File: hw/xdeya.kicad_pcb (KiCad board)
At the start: 2 copper layers, 86.2 x 48.5 mm, 75 parts, among them J2 display, J3 antenna, J4 USB_B_Micro, J5 battery, J6 A, J7 K, Q1 ML5203, Q2 ML5203, Q3 S8050, Q4 S8050, SW3 btn-up, SW4 btn-sel, SW5 btn-down, U1 ESP32-WROOM-32, U2 MCP73831, U3 MIC5219-3.3, U4 BMP280, U5 PCF8563T, U6 NEO-M8N, U7 CP2102, U8 LSM303DLH, U9 XC6206P182MR, Y1 32768

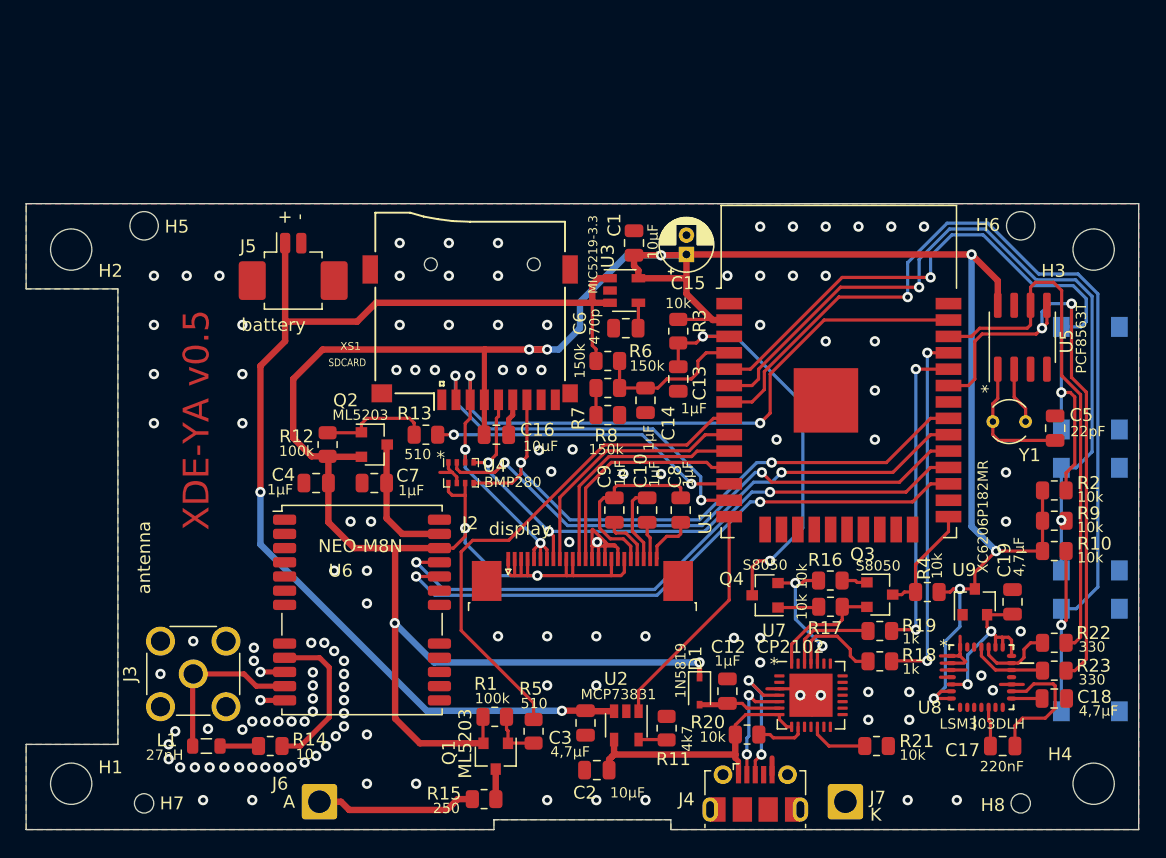
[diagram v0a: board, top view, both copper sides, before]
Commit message: hw - обновление kikad до v7
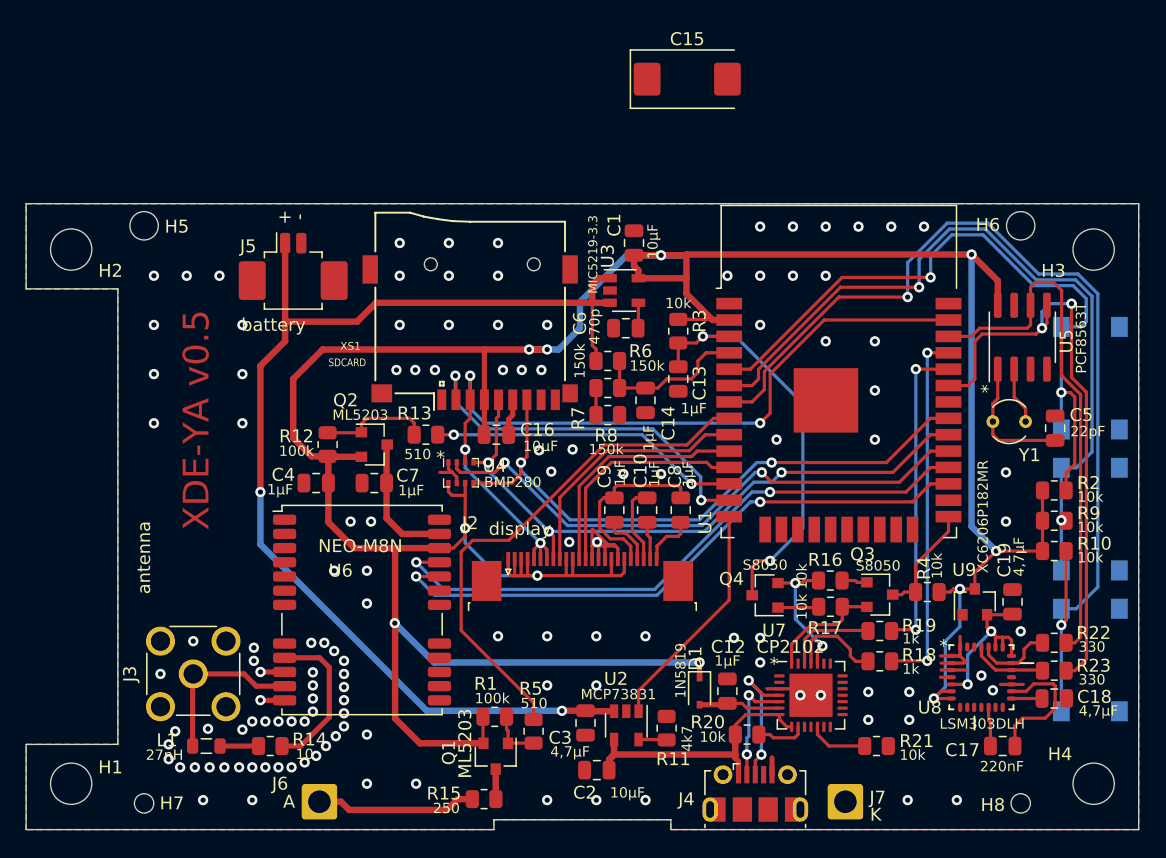
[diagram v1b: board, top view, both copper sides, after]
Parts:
- C15: value CP -> 330uf; footprint Capacitor_THT:CP_Radial_D4.0mm_P1.50mm -> Capacitor_Tantalum_SMD:CP_EIA-7343-20_Kemet-V
- moved C15 13.6 mm to (101.0, 27.9), turned to 0 degrees
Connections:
- C1 pad 1: +3V3 -> +3.3V
- C13 pad 1: /s-en -> +3.3V
- C15 pad 1: +3V3 -> +3.3V
- C16 pad 1: +3V3 -> +3.3V
- C4 pad 1: +3V3 -> +3.3V
- D1 pad 1: +3V3 -> +3.3V
- J2 pad 1: +3V3 -> +3.3V
- J2 pad 10: +3V3 -> +3.3V
- J2 pad 11: +3V3 -> +3.3V
- J2 pad 17: +3V3 -> +3.3V
- J2 pad 19: +3V3 -> +3.3V
- J2 pad 2: +3V3 -> +3.3V
- J2 pad 3: +3V3 -> +3.3V
- J2 pad 4: +3V3 -> +3.3V
- J4 pad 4: Net-(J4-Pad4) -> unconnected-(J4-ID-Pad4)
- Q1 pad 2: +3V3 -> +3.3V
- Q2 pad 2: +3V3 -> +3.3V
- Q4 pad 2: Net-(Q4-Pad2) -> Net-(Q4-E)
- Q4 pad 3: /s-en -> +3.3V
- R1 pad 1: +3V3 -> +3.3V
- R10 pad 1: +3V3 -> +3.3V
- R12 pad 1: +3V3 -> +3.3V
- R16 pad 2: Net-(Q4-Pad2) -> Net-(Q4-E)
- R18 pad 1: Net-(R18-Pad1) -> Net-(U7-~{RTS})
- R19 pad 1: Net-(R19-Pad1) -> Net-(U7-~{CTS})
- R2 pad 1: +3V3 -> +3.3V
- R20 pad 2: Net-(R20-Pad2) -> unconnected-(R20-Pad2)
- R21 pad 1: Net-(R21-Pad1) -> Net-(U7-~{SUSPEND})
- R3 pad 1: +3V3 -> +3.3V
- R3 pad 2: /s-en -> +3.3V
- R4 pad 1: +3V3 -> +3.3V
- R9 pad 1: +3V3 -> +3.3V
- U1 pad 16: Net-(U1-Pad16) -> unconnected-(U1-IO13-Pad16)
- U1 pad 17: Net-(U1-Pad17) -> unconnected-(U1-SHD/SD2-Pad17)
- U1 pad 18: Net-(U1-Pad18) -> unconnected-(U1-SWP/SD3-Pad18)
- U1 pad 19: Net-(U1-Pad19) -> unconnected-(U1-SCS/CMD-Pad19)
- U1 pad 2: +3V3 -> +3.3V
- U1 pad 20: Net-(U1-Pad20) -> unconnected-(U1-SCK/CLK-Pad20)
- U1 pad 21: Net-(U1-Pad21) -> unconnected-(U1-SDO/SD0-Pad21)
- U1 pad 22: Net-(U1-Pad22) -> unconnected-(U1-SDI/SD1-Pad22)
- U1 pad 23: Net-(U1-Pad23) -> unconnected-(U1-IO15-Pad23)
- U1 pad 24: Net-(U1-Pad24) -> unconnected-(U1-IO2-Pad24)
- U1 pad 26: Net-(U1-Pad26) -> unconnected-(U1-IO4-Pad26)
- U1 pad 3: /s-en -> +3.3V
- U1 pad 32: Net-(U1-Pad32) -> unconnected-(U1-NC-Pad32)
- U3 pad 5: +3V3 -> +3.3V
- U4 pad 6: +3V3 -> +3.3V
- U4 pad 8: +3V3 -> +3.3V
- U5 pad 3: Net-(U5-Pad3) -> unconnected-(U5-~{INT}-Pad3)
- U5 pad 7: Net-(U5-Pad7) -> unconnected-(U5-CLKO-Pad7)
- U5 pad 8: +3V3 -> +3.3V
- U6 pad 1: Net-(U6-Pad1) -> unconnected-(U6-~{SAFEBOOT}-Pad1)
- U6 pad 14: Net-(U6-Pad14) -> unconnected-(U6-LNA_EN-Pad14)
- U6 pad 15: Net-(U6-Pad15) -> unconnected-(U6-RESERVED-Pad15)
- U6 pad 16: Net-(U6-Pad16) -> unconnected-(U6-RESERVED-Pad16)
- U6 pad 17: Net-(U6-Pad17) -> unconnected-(U6-RESERVED-Pad17)
- U6 pad 18: Net-(U6-Pad18) -> unconnected-(U6-SDA/~{SPI_CS}-Pad18)
- U6 pad 19: Net-(U6-Pad19) -> unconnected-(U6-SCL/SPI_CLK-Pad19)
- U6 pad 2: Net-(U6-Pad2) -> unconnected-(U6-D_SEL-Pad2)
- U6 pad 22: +3V3 -> +3.3V
- U6 pad 3: Net-(U6-Pad3) -> unconnected-(U6-TIMEPULSE-Pad3)
- U6 pad 4: Net-(U6-Pad4) -> unconnected-(U6-EXTINT-Pad4)
- U6 pad 5: Net-(U6-Pad5) -> unconnected-(U6-USB_DM-Pad5)
- U6 pad 6: Net-(U6-Pad6) -> unconnected-(U6-USB_DP-Pad6)
- U6 pad 8: Net-(U6-Pad8) -> unconnected-(U6-~{RESET}-Pad8)
- U7 pad 1: Net-(U7-Pad1) -> unconnected-(U7-~{DCD}-Pad1)
- U7 pad 10: Net-(U7-Pad10) -> unconnected-(U7-NC-Pad10)
- U7 pad 11: Net-(U7-Pad11) -> Net-(U7-~{SUSPEND})
- U7 pad 12: Net-(R21-Pad1) -> unconnected-(U7-SUSPEND-Pad12)
- U7 pad 13: Net-(U7-Pad13) -> unconnected-(U7-CHREN-Pad13)
- U7 pad 14: Net-(U7-Pad14) -> unconnected-(U7-CHR1-Pad14)
- U7 pad 15: Net-(U7-Pad15) -> unconnected-(U7-CHR0-Pad15)
- U7 pad 16: Net-(U7-Pad16) -> unconnected-(U7-~{WAKEUP}/GPIO.3-Pad16)
- U7 pad 17: Net-(U7-Pad17) -> unconnected-(U7-RS485/GPIO.2-Pad17)
- U7 pad 18: Net-(U7-Pad18) -> unconnected-(U7-~{RXT}/GPIO.1-Pad18)
- U7 pad 19: Net-(U7-Pad19) -> unconnected-(U7-~{TXT}/GPIO.0-Pad19)
- U7 pad 2: Net-(U7-Pad2) -> unconnected-(U7-~{RI}/CLK-Pad2)
- U7 pad 20: Net-(U7-Pad20) -> unconnected-(U7-GPIO.6-Pad20)
- U7 pad 21: Net-(U7-Pad21) -> unconnected-(U7-GPIO.5-Pad21)
- U7 pad 22: Net-(U7-Pad22) -> unconnected-(U7-GPIO.4-Pad22)
- U7 pad 23: Net-(U7-Pad23) -> Net-(U7-~{CTS})
- U7 pad 24: Net-(Q4-Pad2) -> Net-(U7-~{RTS})
- U7 pad 25: Net-(R18-Pad1) -> Net-(Q4-E)
- U7 pad 26: Net-(R19-Pad1) -> unconnected-(U7-TXD-Pad26)
- U7 pad 27: Net-(U7-Pad27) -> unconnected-(U7-~{DSR}-Pad27)
- U7 pad 4: /usb-d+ -> unconnected-(U7-D+-Pad4)
- U7 pad 8: /usb-5v -> /usb-d+
- U7 pad 9: Net-(R20-Pad2) -> unconnected-(U7-~{RST}-Pad9)
- U8 pad 10: Net-(U8-Pad10) -> unconnected-(U8-RES_5-Pad10)
- U8 pad 11: Net-(U8-Pad11) -> unconnected-(U8-RES_7-Pad11)
- U8 pad 13: Net-(U8-Pad13) -> unconnected-(U8-RES_8-Pad13)
- U8 pad 14: Net-(U8-Pad14) -> unconnected-(U8-RES_6-Pad14)
- U8 pad 18: Net-(U8-Pad18) -> unconnected-(U8-DRDY_M-Pad18)
- U8 pad 26: Net-(U8-Pad26) -> unconnected-(U8-INT1-Pad26)
- U8 pad 27: Net-(U8-Pad27) -> unconnected-(U8-INT2-Pad27)
- U8 pad 6: +3V3 -> +3.3V
- U8 pad 7: +3V3 -> +3.3V
- U8 pad 8: Net-(U8-Pad8) -> unconnected-(U8-NC_2-Pad8)
- U8 pad 9: Net-(U8-Pad9) -> unconnected-(U8-NC-Pad9)
- U9 pad 3: +3V3 -> +3.3V
- XS1 pad 1: Net-(XS1-Pad1) -> unconnected-(XS1-DAT2-Pad1)
- XS1 pad 4: +3V3 -> +3.3V
- XS1 pad 8: Net-(XS1-Pad8) -> unconnected-(XS1-DAT1-Pad8)
- XS1 pad 9: Net-(XS1-Pad9) -> unconnected-(XS1-CD-Pad9)
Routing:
- net +3.3V: track 0.00 -> 283.4 mm, vias 0 -> 13
- net +3V3: track 250.5 -> 0.00 mm, vias 11 -> 0
- net (no net): track 0.00 -> 33.5 mm, vias 0 -> 2
- net /s-en: track 32.9 -> 0.00 mm, vias 2 -> 0
- net Net-(Q4-Pad2): track 10.5 -> 0.00 mm, vias 2 -> 0
- net Net-(R18-Pad1): track 7.42 -> 0.00 mm
- net Net-(R19-Pad1): track 7.10 -> 0.00 mm
- net Net-(R21-Pad1): track 4.63 -> 0.00 mm
- net Net-(R20-Pad2): track 3.84 -> 0.00 mm
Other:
- net class Default removed

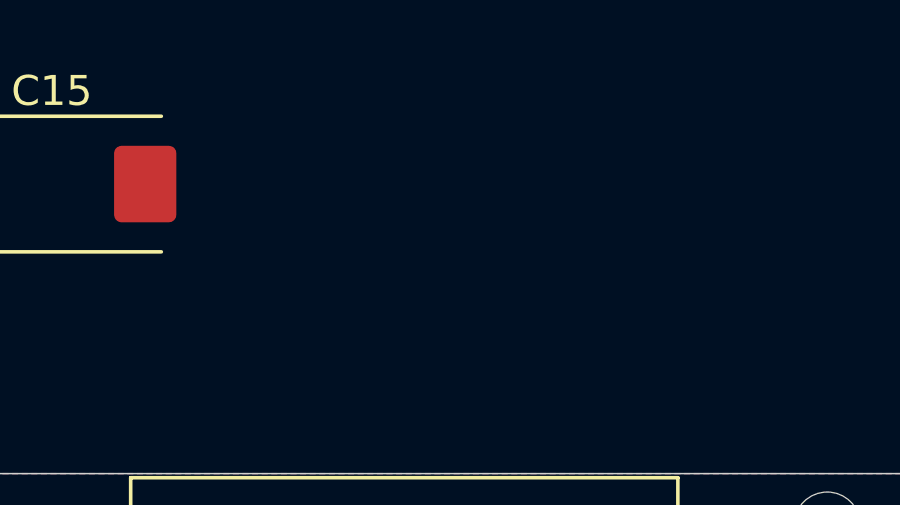
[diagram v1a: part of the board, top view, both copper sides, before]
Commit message: hw - схема с использованием axp2101
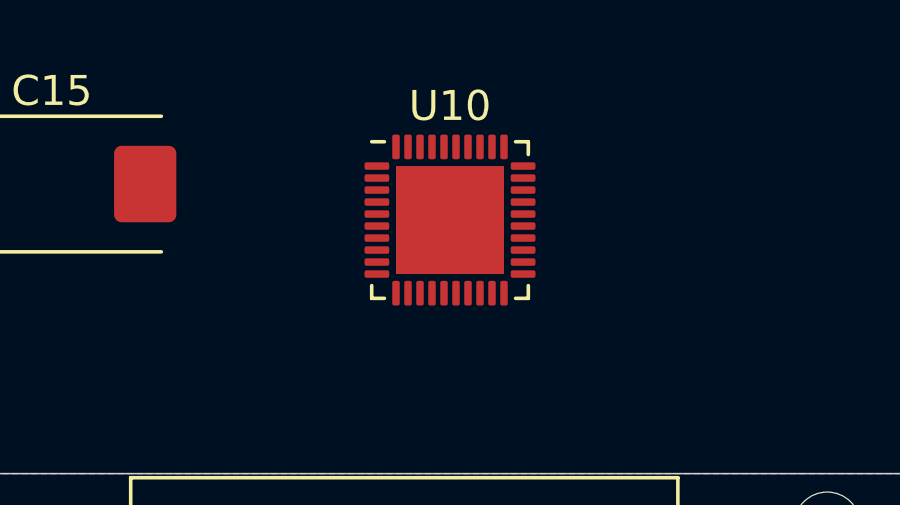
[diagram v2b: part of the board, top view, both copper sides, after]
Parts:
- added U10: AXP2101, Package_DFN_QFN:QFN-40-1EP_5x5mm_P0.4mm_EP3.6x3.6mm, F.Cu at (114.3, 29.1)

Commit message: hw - примерная расстановка элементов
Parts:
- removed C12, C14: 1μF, Capacitor_SMD:C_0805_2012Metric
- removed C18: 4,7μF, Capacitor_SMD:C_0805_2012Metric
- removed D1: 1N5819, Diode_SMD:D_SOD-323
- removed Q1, Q2: ML5203, Package_TO_SOT_SMD:SOT-23
- removed Q3, Q4: S8050, Package_TO_SOT_SMD:SOT-23
- removed R1, R12: 100k, Resistor_SMD:R_0805_2012Metric
- removed R13, R5: 510, Resistor_SMD:R_0805_2012Metric
- removed R6, R7, R8: 150k, Resistor_SMD:R_0805_2012Metric
- removed U3: MIC5219-3.3, Package_TO_SOT_SMD:SOT-23-5
- removed U8: LSM303DLH, lsm303dlh:LGA28R55P7X7_500X500X100
- removed U9: XC6206P182MR, Package_TO_SOT_SMD:SOT-23
- added C11: 10μF, Capacitor_SMD:C_0805_2012Metric, F.Cu at (120.0, 77.2)
- added C20: 10μF, Capacitor_SMD:C_0805_2012Metric, F.Cu at (106.1, 68.5)
- added C21: 10μF, Capacitor_SMD:C_0805_2012Metric, F.Cu at (113.0, 68.5)
- added C22: 22μF, Capacitor_SMD:C_0805_2012Metric, F.Cu at (103.9, 68.5)
- added C23: 10μF, Capacitor_SMD:C_0805_2012Metric, F.Cu at (115.3, 68.5)
- added C24: 1μF, Capacitor_SMD:C_0805_2012Metric, F.Cu at (120.0, 74.8)
- added C25: 1μF, Capacitor_SMD:C_0805_2012Metric, F.Cu at (120.0, 72.4)
- added C26: 1μF, Capacitor_SMD:C_0805_2012Metric, F.Cu at (129.7, 47.1)
- added C27: 4,7μF, Capacitor_SMD:C_0805_2012Metric, F.Cu at (79.2, 57.4)
- added D2: 1N5819, Diode_SMD:D_SOD-323, F.Cu at (94.2, 71.8)
- added L2: 2.2μH/1.5A, Inductor_SMD_Wurth:L_Wurth_WE-LQSH-3012, F.Cu at (104.8, 72.5)
- added Q5: UMH3N, Package_TO_SOT_SMD:SOT-363_SC-70-6, F.Cu at (90.5, 71.5)
- added R24: 47k, Resistor_SMD:R_0805_2012Metric, F.Cu at (109.2, 74.4)
- C3: value 4,7μF -> 10μF
- C6: value 470p -> 1μF
- C7: value 1μF -> 4,7μF
- R11: value 4k7 -> 100
- R16, R17: value 10k -> 1
- U2: value MCP73831 -> LSM303AGR; footprint Package_TO_SOT_SMD:SOT-23-5 -> lsm303agr:PQFN50P200X200X100-12N
- Y1: footprint Crystal:Crystal_AT310_D3.0mm_L10.0mm_Vertical -> Crystal:Crystal_DS26_D2.0mm_L6.0mm_Horizontal_1EP_style2
- moved C7 50.2 mm to (126.2, 67.9), turned to 90 degrees
- moved U10 45.4 mm to (114.6, 74.5), turned to 180 degrees
- moved U2 28.7 mm to (124.5, 72.3), turned to 0 degrees
- moved C6 26.1 mm to (87.2, 71.8), turned to -90 degrees
- moved R21 22.8 mm to (93.2, 83.2)
- moved R19 21.5 mm to (95.8, 78.2)
- moved U7 20.7 mm to (90.2, 78.7)
- moved R18 20.4 mm to (95.8, 76.0)
- moved C15 19.9 mm to (95.8, 47.1), turned to -90 degrees
- moved C4 17.6 mm to (84.7, 71.8), turned to -90 degrees
- moved R20 16.7 mm to (89.6, 83.2)
- moved C3 16.1 mm to (109.2, 79.0), turned to 180 degrees
- moved R11 9.91 mm to (109.2, 76.7), turned to 0 degrees
- moved C2 9.26 mm to (84.8, 80.3)
- moved C17 7.96 mm to (127.8, 72.0), turned to 90 degrees
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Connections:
- net /usb-d- renamed Net-(J4-D-)
- C13 pad 1: +3.3V -> /s-en
- C16 pad 1: +3.3V -> VSDCARD
- C17 pad 1: Net-(U8-SET1) -> Net-(U2-C1)
- C17 pad 2: Net-(U8-SET2) -> GND
- C19 pad 1: +1V8 -> VCOMP-IO
- C2 pad 1: /usb-5v -> VBUS
- C3 pad 1: +BATT -> Net-(J5-Pin_1)
- C4 pad 1: +3.3V -> VRTC
- C6 pad 1: Net-(U3-BP) -> VNAVI
- C7 pad 1: hwpwr -> VCOMP-SUPP
- J4 pad 1: /usb-5v -> VBUS
- J4 pad 3: /usb-d+ -> Net-(J4-D+)
- J5 pad 1: +BATT -> Net-(J5-Pin_1)
- R11 pad 1: Net-(U2-PROG) -> GND
- R11 pad 2: GND -> Net-(U10-TS)
- R15 pad 2: Net-(Q1-D) -> DLIGHT
- R16 pad 1: Net-(Q3-B) -> Net-(U10-ALDOIN)
- R16 pad 2: Net-(Q4-E) -> VSYS
- R17 pad 1: Net-(Q3-E) -> Net-(U10-BLDOIN)
- R17 pad 2: Net-(Q4-B) -> VSYS
- R18 pad 1: Net-(U7-~{RTS}) -> Net-(U7-TXD)
- R19 pad 1: Net-(U7-~{CTS}) -> Net-(U7-RXD)
- R20 pad 1: /usb-5v -> VBUS
- R20 pad 2: unconnected-(R20-Pad2) -> Net-(U7-~{RST})
- R21 pad 1: Net-(U7-~{SUSPEND}) -> Net-(U7-SUSPEND)
- R22 pad 1: Net-(U8-SCL_A) -> Net-(U2-SCL/SPC)
- R23 pad 2: Net-(U8-SDA_A) -> Net-(U2-SDA/SDI/SDO)
- R3 pad 2: +3.3V -> /s-en
- R9 pad 2: /b-sel -> PWROK
- SW4 pad 2: /b-sel -> PWROK
- U1 pad 12: hwen -> unconnected-(U1-IO27-Pad12)
- U1 pad 14: chg-ind -> unconnected-(U1-IO12-Pad14)
- U1 pad 3: +3.3V -> /s-en
- U1 pad 4: /batt-chk -> CHRGIRQ
- U1 pad 6: /b-sel -> PWROK
- U1 pad 8: d-led -> unconnected-(U1-IO32-Pad8)
- U10 pad 10: unconnected-(U10-CPULDOS-Pad10) -> Net-(U10-CPULDOS)
- U10 pad 12: unconnected-(U10-BLDO1-Pad12) -> VCOMP-IO
- U10 pad 13: unconnected-(U10-BLDOIN-Pad13) -> Net-(U10-BLDOIN)
- U10 pad 14: unconnected-(U10-BLDO2-Pad14) -> VCOMP-SUPP
- U10 pad 15: unconnected-(U10-ALDO4-Pad15) -> VSDCARD
- U10 pad 16: unconnected-(U10-ALDO3-Pad16) -> VNAVI
- U10 pad 17: unconnected-(U10-ALDOIN-Pad17) -> Net-(U10-ALDOIN)
- U10 pad 18: unconnected-(U10-ALDO1-Pad18) -> VBMP
- U10 pad 19: unconnected-(U10-ALDO2-Pad19) -> DLIGHT
- U10 pad 2: unconnected-(U10-VREF-Pad2) -> Net-(U10-VREF)
- U10 pad 21: unconnected-(U10-FB1-Pad21) -> +3.3V
- U10 pad 22: unconnected-(U10-LX1-Pad22) -> Net-(U10-LX1)
- U10 pad 23: unconnected-(U10-VIN1-Pad23) -> VSYS
- U10 pad 28: unconnected-(U10-VRTC-Pad28) -> VRTC
- U10 pad 29: unconnected-(U10-PWROK-Pad29) -> PWROK
- U10 pad 3: unconnected-(U10-GND-Pad3) -> GND
- U10 pad 30: unconnected-(U10-PWRON-Pad30) -> PWRON
- U10 pad 31: unconnected-(U10-TS-Pad31) -> Net-(U10-TS)
- U10 pad 33: unconnected-(U10-BAT-Pad33) -> Net-(J5-Pin_1)
- U10 pad 34: unconnected-(U10-VSYS-Pad34) -> VSYS
- U10 pad 36: unconnected-(U10-VMID-Pad36) -> VSYS
- U10 pad 37: unconnected-(U10-VBUS-Pad37) -> VBUS
- U10 pad 38: unconnected-(U10-IRQ-Pad38) -> CHRGIRQ
- U10 pad 39: unconnected-(U10-SDA-Pad39) -> i2c-sda
- U10 pad 40: unconnected-(U10-SCK-Pad40) -> i2c-scl
- U10 pad 41: unconnected-(U10-GND-Pad41) -> GND
- U2 pad 1: chg-ind -> Net-(U2-SCL/SPC)
- U2 pad 2: GND -> VCOMP-IO
- U2 pad 3: +BATT -> VCOMP-IO
- U2 pad 4: /usb-5v -> Net-(U2-SDA/SDI/SDO)
- U2 pad 5: Net-(U2-PROG) -> Net-(U2-C1)
- U4 pad 6: +3.3V -> VBMP
- U4 pad 8: +3.3V -> VBMP
- U5 pad 8: +3.3V -> VRTC
- U6 pad 22: +3.3V -> VRTC
- U6 pad 23: hwpwr -> VNAVI
- U7 pad 11: Net-(U7-~{SUSPEND}) -> unconnected-(U7-~{SUSPEND}-Pad11)
- U7 pad 12: unconnected-(U7-SUSPEND-Pad12) -> Net-(U7-SUSPEND)
- U7 pad 23: Net-(U7-~{CTS}) -> unconnected-(U7-~{CTS}-Pad23)
- U7 pad 24: Net-(U7-~{RTS}) -> Net-(Q5A-E1)
- U7 pad 25: Net-(Q4-E) -> Net-(U7-RXD)
- U7 pad 26: unconnected-(U7-TXD-Pad26) -> Net-(U7-TXD)
- U7 pad 28: Net-(Q3-E) -> Net-(Q5A-B1)
- U7 pad 4: unconnected-(U7-D+-Pad4) -> Net-(J4-D+)
- U7 pad 6: Net-(D1-A) -> unconnected-(U7-VDD-Pad6)
- U7 pad 7: /usb-5v -> VBUS
- U7 pad 8: /usb-d+ -> VBUS
- U7 pad 9: unconnected-(U7-~{RST}-Pad9) -> Net-(U7-~{RST})
- XS1 pad 4: +3.3V -> VSDCARD
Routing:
- net +3.3V: track 283.4 -> 35.9 mm, vias 13 -> 0
- net +BATT: track 90.3 -> 0.00 mm, vias 2 -> 0
- net PWROK: track 0.00 -> 59.9 mm, vias 0 -> 1
- net /b-sel: track 59.9 -> 0.00 mm, vias 2 -> 0
- net d-led: track 40.4 -> 0.00 mm
- net i2c-sda: track 46.5 -> 12.7 mm, vias 2 -> 0
- net (no net): track 33.5 -> 0.00 mm, vias 2 -> 0
- net hwen: track 24.2 -> 0.00 mm, vias 2 -> 0
- net i2c-scl: track 41.3 -> 19.3 mm
- net /usb-5v: track 21.2 -> 0.00 mm
- net GND: track 34.8 -> 15.7 mm, vias 125 -> 88
- net chg-ind: track 18.0 -> 0.00 mm
- net +1V8: track 14.3 -> 0.00 mm, vias 2 -> 0
- net Net-(J6-Pin_1): track 12.5 -> 0.00 mm
- net /batt-chk: track 12.2 -> 0.00 mm
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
